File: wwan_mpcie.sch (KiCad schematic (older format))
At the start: 45 parts, among them J1501 u.FL, J1502 u.FL, J1503 MPCIE-Socket, J1504 Micro_SIM_Card, Q1501 FDV301N, SW1501 WWAN_HKS, U1501 NTB0104GU12, U1502 NUP5120, U1503 74LVC1G08, U1504 74LVC1G86

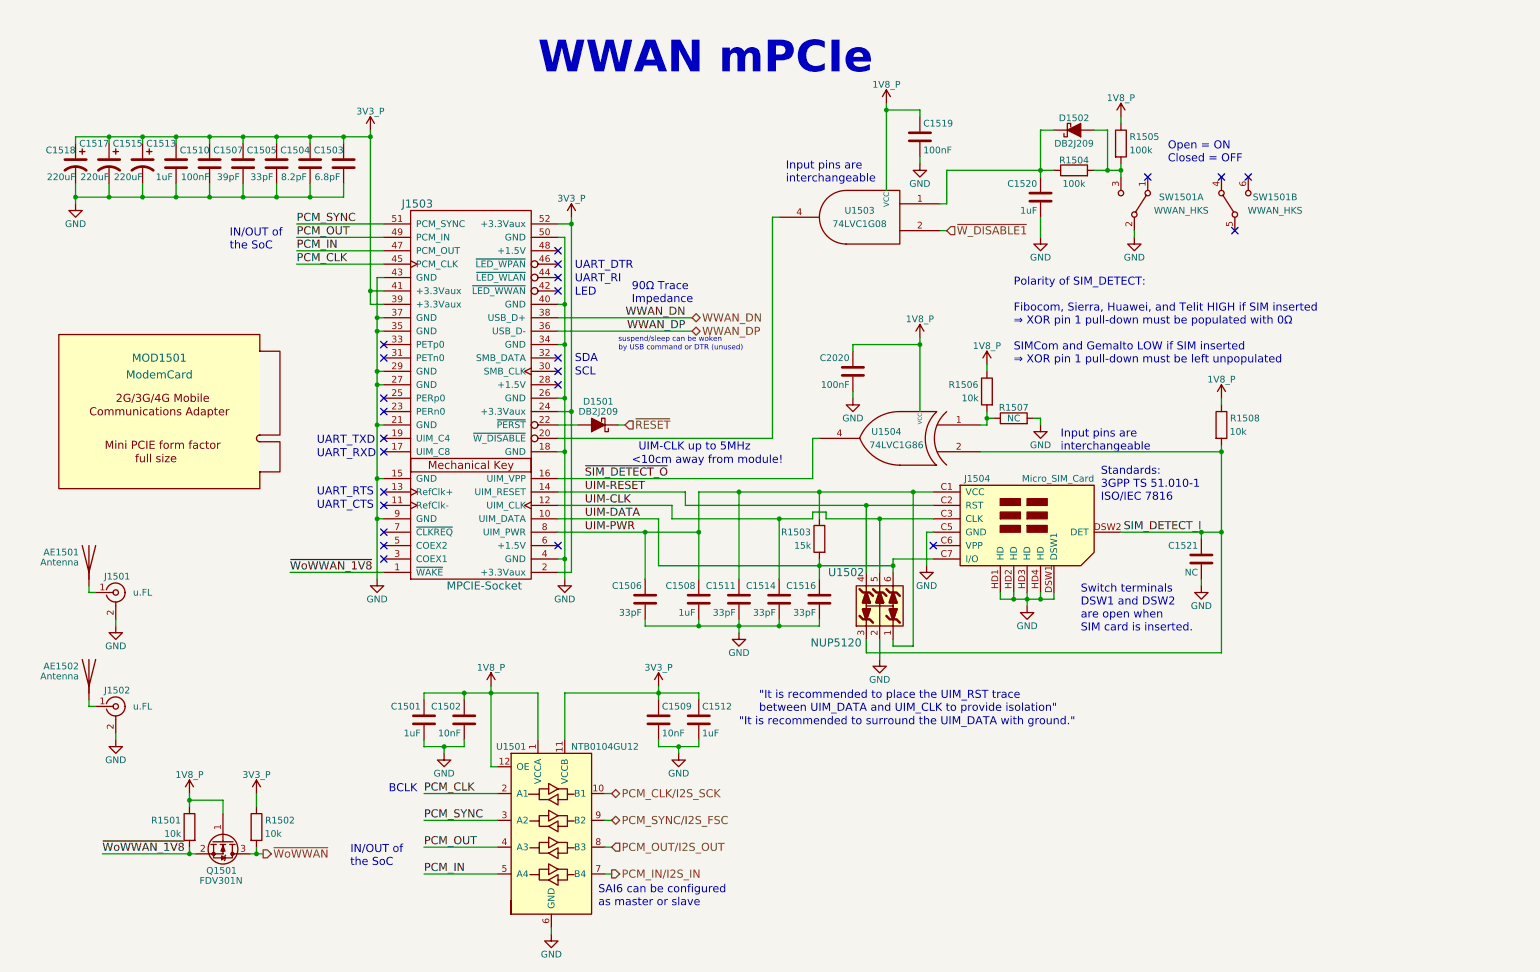
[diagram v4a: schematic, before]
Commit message: Assign "mpcie-outline" footprint to the ModemCard schematic symbol
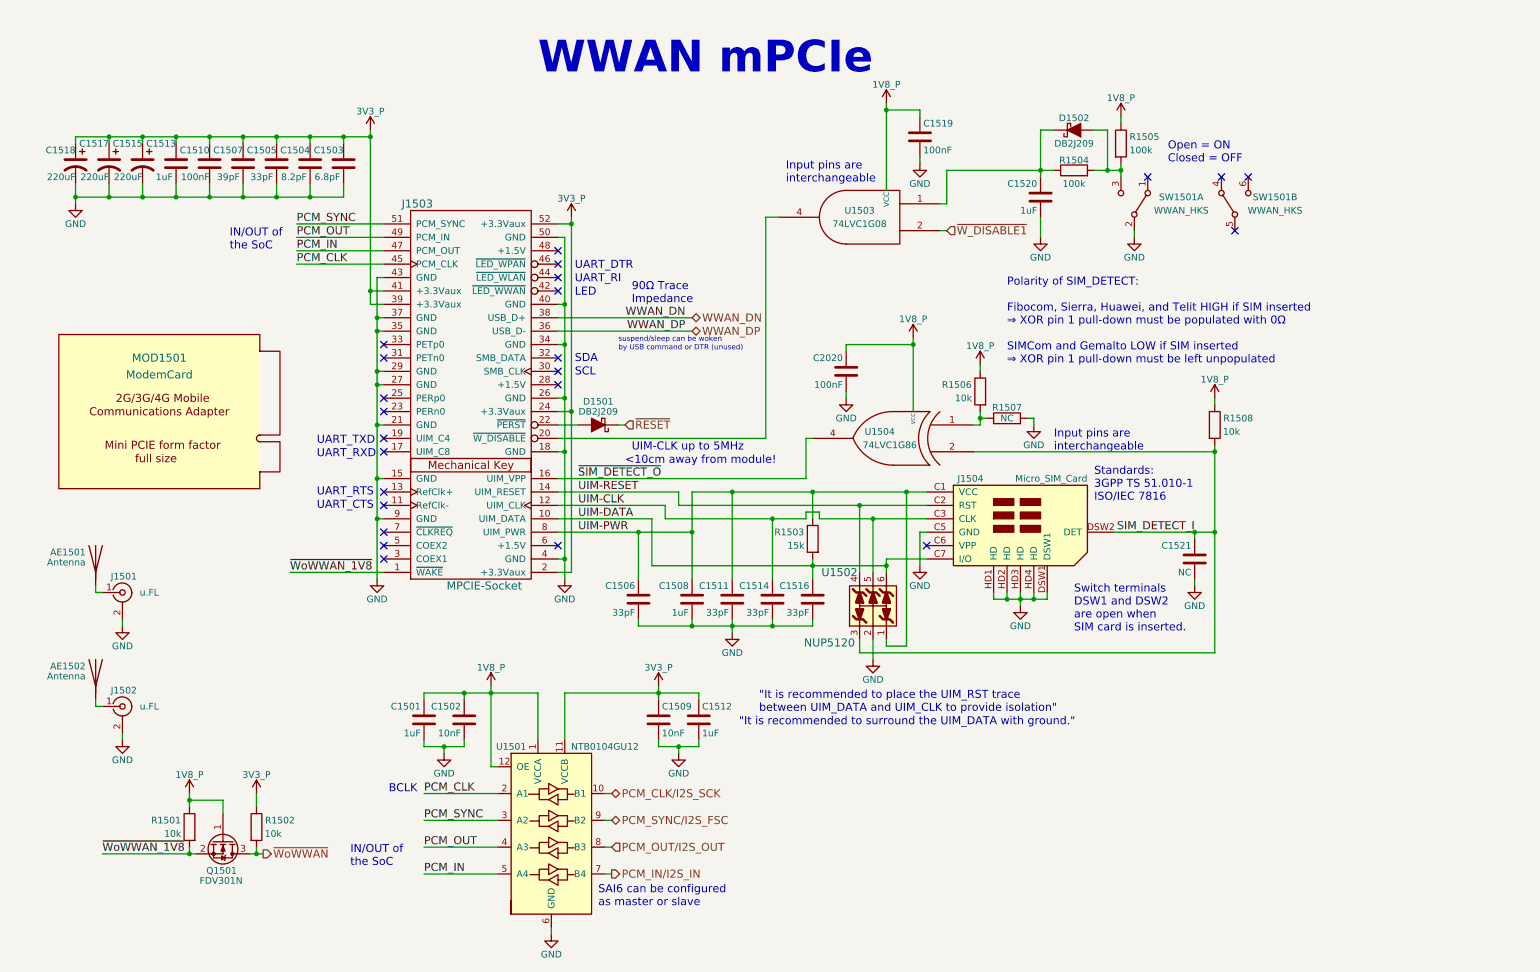
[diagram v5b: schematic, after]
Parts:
- MOD1501: footprint (none) -> dvk-mx8m-bsb:mpcie-outline
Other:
- moved on the sheet: AE1501, AE1502, C1506, C1508, C1511, C1514, C1516, C1521, C2020, J1501, J1502, J1504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

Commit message: Make a few minor aesthetic adjustments to the schematic
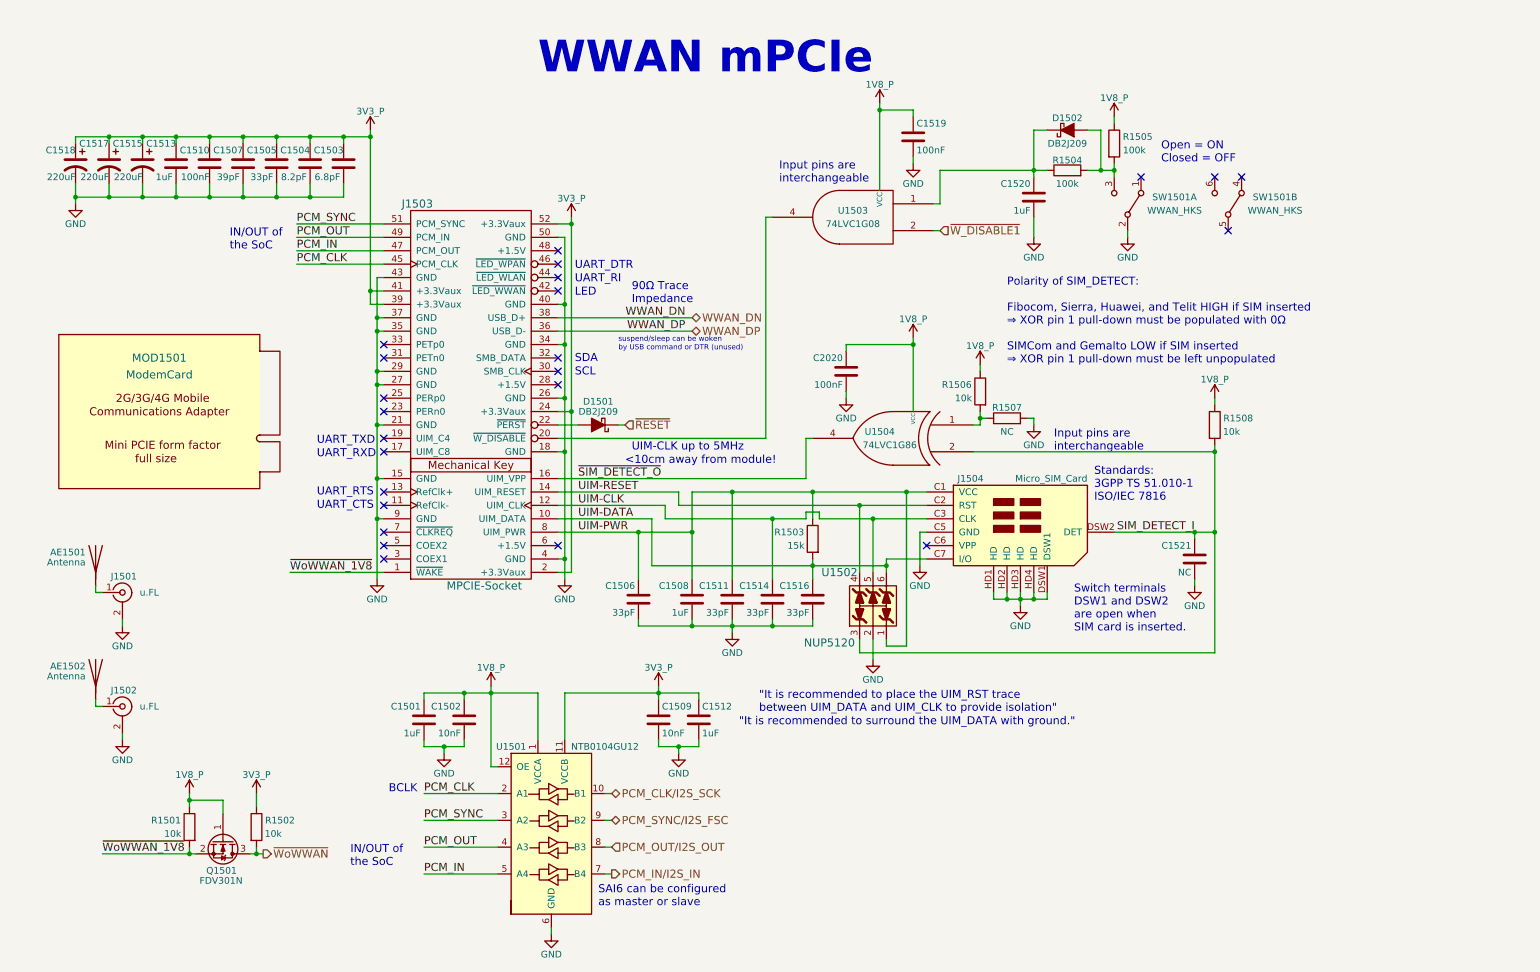
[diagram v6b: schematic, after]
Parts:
- J1503: MFG Part Num (none) -> 2041119-1; MFG Part Number 2041119-1 -> (none)
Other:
- moved on the sheet: C1519, C1520, D1502, R1504, R1505, SW1501A, SW1501B, U1503

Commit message: Add mounting holes to the schematic and assign the associated M2 hole footprint, add fiducial marks to schematic and assign the associated 1mm diameter copper with 2mm diameter solder mask opening footprint, make various visual adjustments throughout the schematic
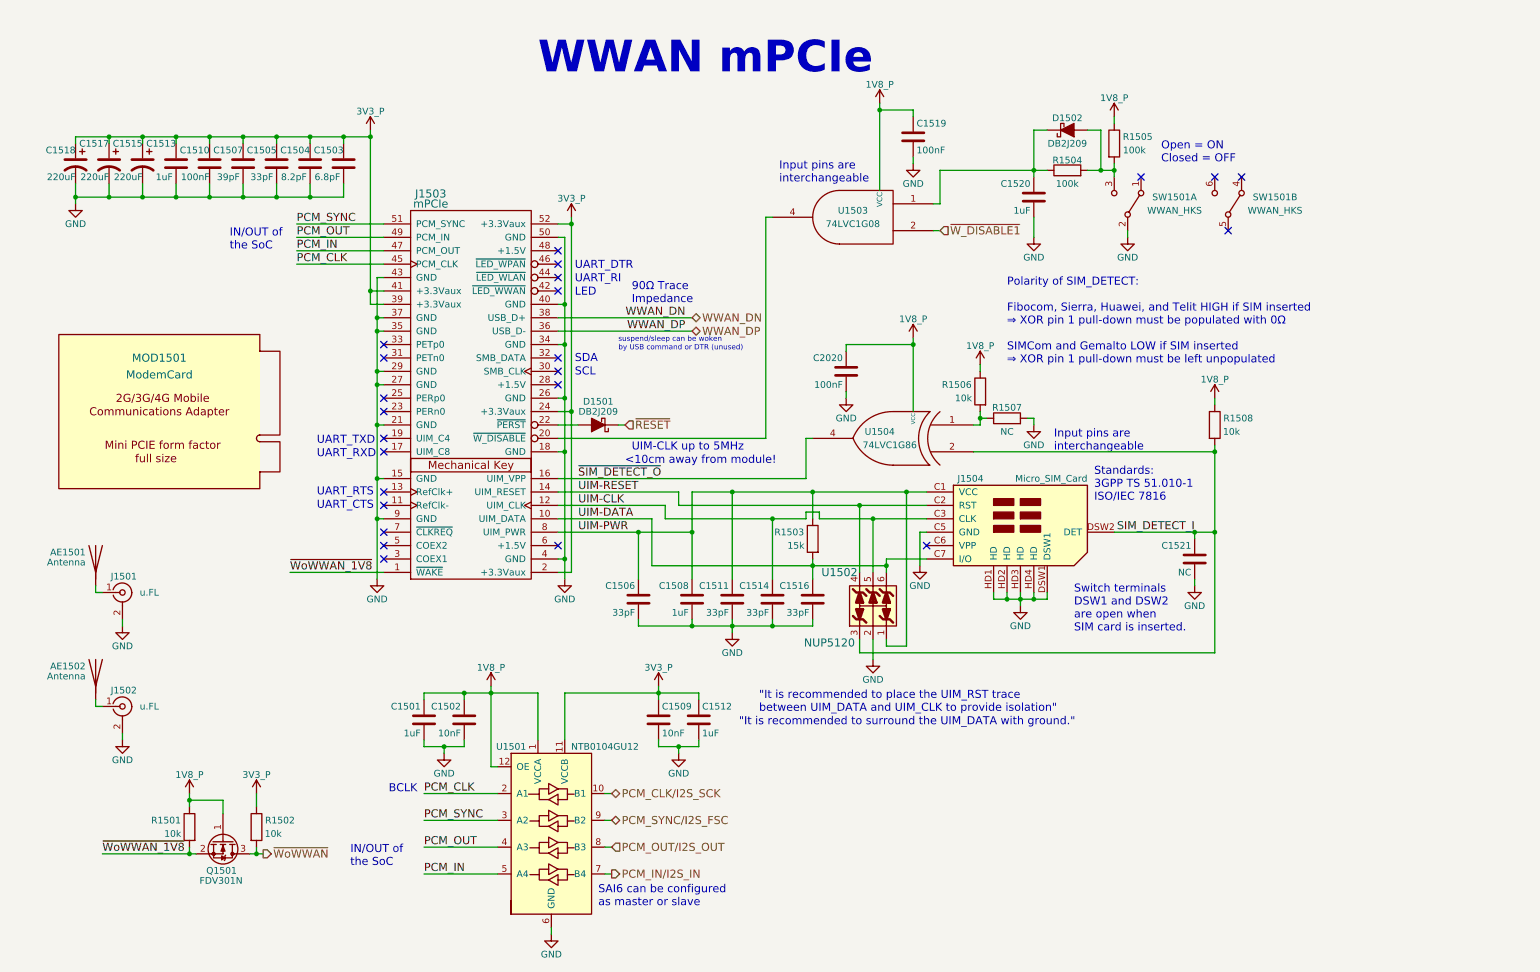
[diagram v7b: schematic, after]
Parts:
- J1503: value MPCIE-Socket -> mPCIe

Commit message: added library symbol for short internal coaxial cables (from u.FL connector of M.2/MiniPCIE Card to ceramic antenna). This component is not appearing at the pcb. The library symbols serves only as a memory aid. Supplier information can be linked to it and should appear then on the BoM.
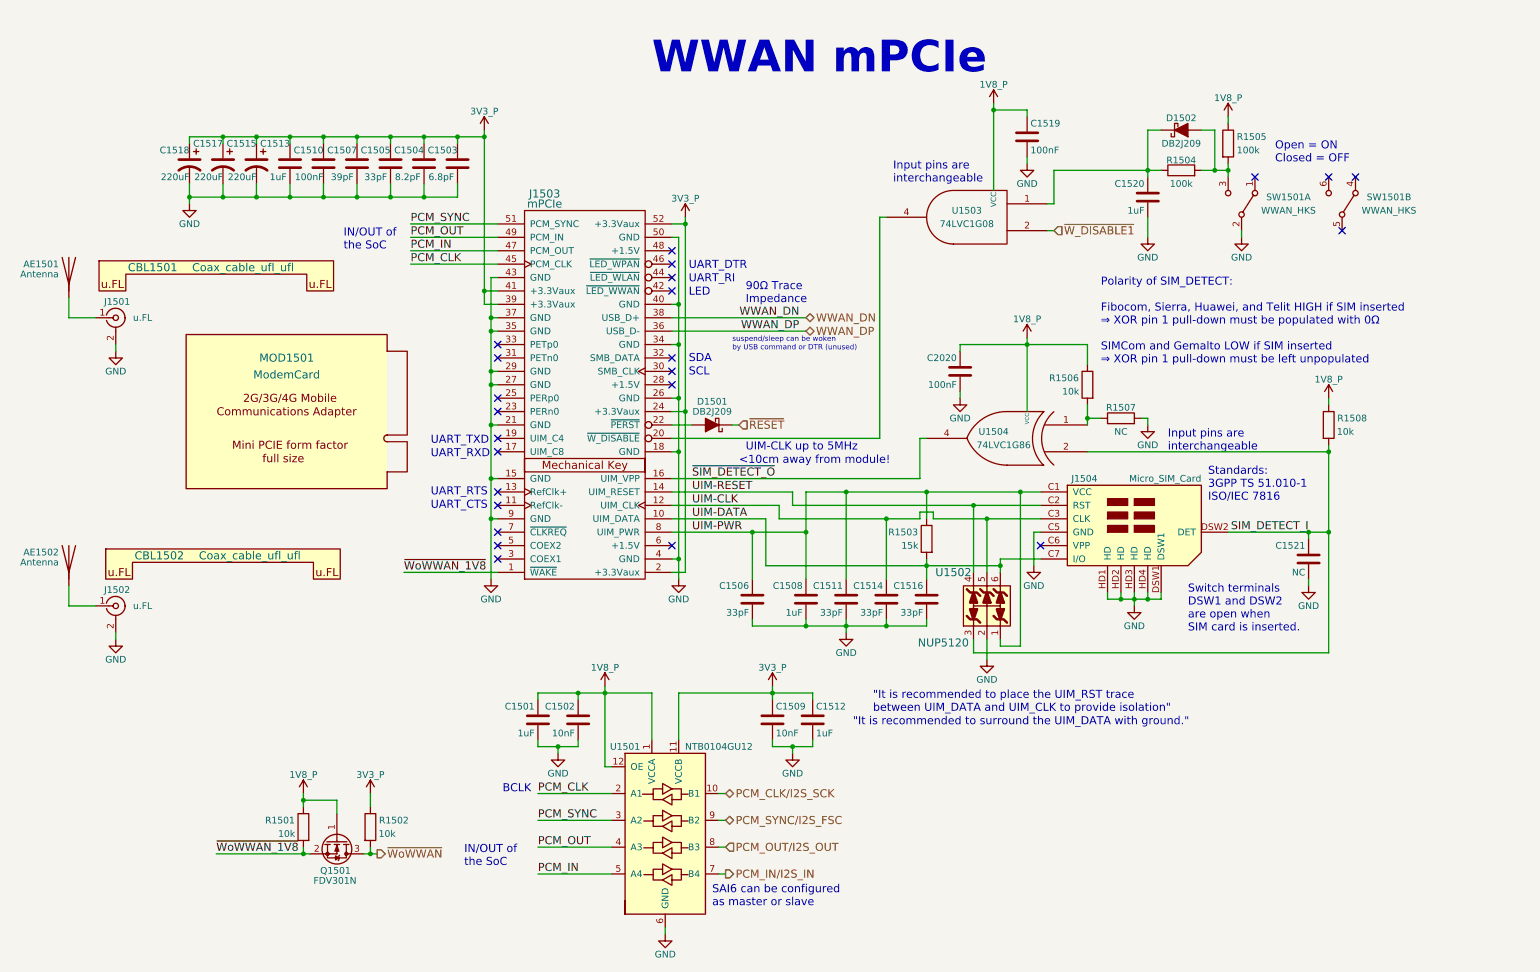
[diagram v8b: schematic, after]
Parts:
- added CBL1501, CBL1502: Coax_cable_ufl_ufl, symbol Coax_cable_ufl_ufl
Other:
- moved on the sheet: AE1501, AE1502, C1501, C1502, C1503, C1504, C1505, C1506, C1507, C1508, C1509, C1510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
